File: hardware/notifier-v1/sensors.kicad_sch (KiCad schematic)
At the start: 7 parts, among them U4 BME688, U5 SHT40-AD1B

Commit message: Sensor neck: no plane under island/neck, guarded 0.15 mm bus, wider slot
- In1 GND left out under the sensor island and neck; the neck bus is
  3V3 | GND | SDA | SCL | GND at 0.15 mm, guards joined on B.Cu and
  stitched to In1 below the neck
- Module-side slot widened to 1.8 mm (island side stays 1.2 mm)
- Island hand-routed and locked (deterministic, clear of SHT40 keepout)
- C12 4.7u bulk cap where 3V3 enters the island
- R13 33R in series with LCD_SCLK (new net MCU_LCD_SCLK), GND vias
  beside the SPI layer changes where there is room
- In2 island removal drops slivers between the module thermal vias

Co-Authored-By: Claude Opus 5.5 <noreply@anthropic.com>
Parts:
- added C12: 4.7u, Capacitor_SMD:C_0603_1608Metric, symbol Device:C
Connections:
- net +3V3: now also C12.1
- net GND: now also C12.2
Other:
- note added: "Notes - BME688: gas and pressure only. Its gas heater self-heats, so T/RH come from the SHT40 away from it. - I2C addresses: BME688 0x77 (SDO high), SHT40 0x44. CSB high selects I2C. - 4.7k pull-ups sit at the bus entry; no pours on the sensor island. - C12 4.7u bulk where 3V3 enters the island."
- note removed: "Notes - BME688: gas and pressure only. Its gas heater self-heats, so T/RH come from the SHT40 away from it. - I2C addresses: BME688 0x77 (SDO high), SHT40 0x44. CSB high selects I2C. - 4.7k pull-ups sit at the bus entry; no pours on the sensor island."

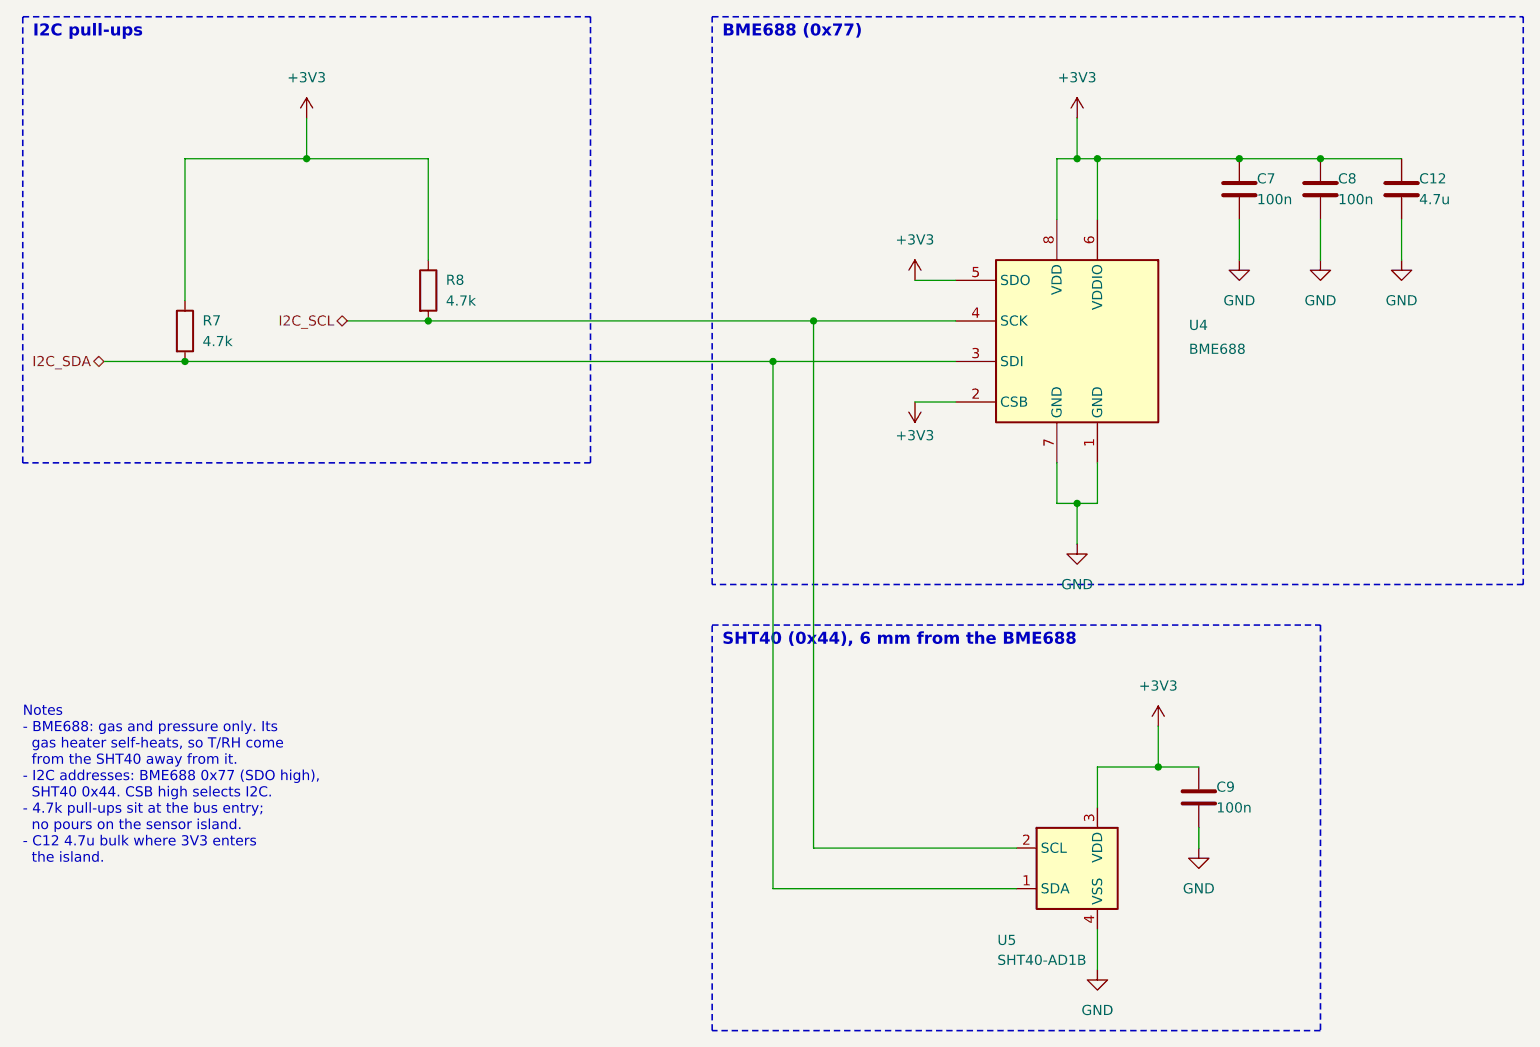
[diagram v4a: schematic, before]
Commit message: Layout A: USB-C on the back edge, corner mounts, no buttons, JLC fab data
- J2 display socket mirrored (1 RST 2 CS 3 DC 4 SDA 5 SCL 6 GND 7 VCC),
  face at the right edge
- USB-C J1 on the left edge (enclosure back), ESD/CC/fuse beside it,
  hand-drawn 0.27/0.15 pair (~91 ohm diff, tools/impedance.py), only
  GND under the shell (DRC rule area)
- SW1-SW3/R6/BTN removed; 1.5 mm debug pads TX RX 3V3 EN GND IO0;
  firmware DESK_BTN = -1 on notifier-v1
- Four M2 corner holes with keepouts; sensor island grown to 14.8 mm
  with H3 in its corner, re-hand-routed (BME688/SHT40 8.9 mm apart)
- I2C >= 1.6 mm from USB on the same layer; vias >= 0.15 mm from
  same-net SMD pads (rule), hand vias >= 0.2 mm
- Silk "v1 ${GIT_SHA}" resolved at fab export; JLC order-number mark
- Fab: Protel gerbers without X2, PTH/NPTH split, JLC BOM/CPL, CPL
  rotation fixes (U4 +90, U5 +270); pipeline --fab-only on a clean
  commit; route retry until the gate passes
- ORDER.md: stackup JLC04161H-7628, rails left/right, preview checklist,
  bring-up without buttons; PLAN.md enclosure notes

Co-Authored-By: Claude Opus 5.5 <noreply@anthropic.com>
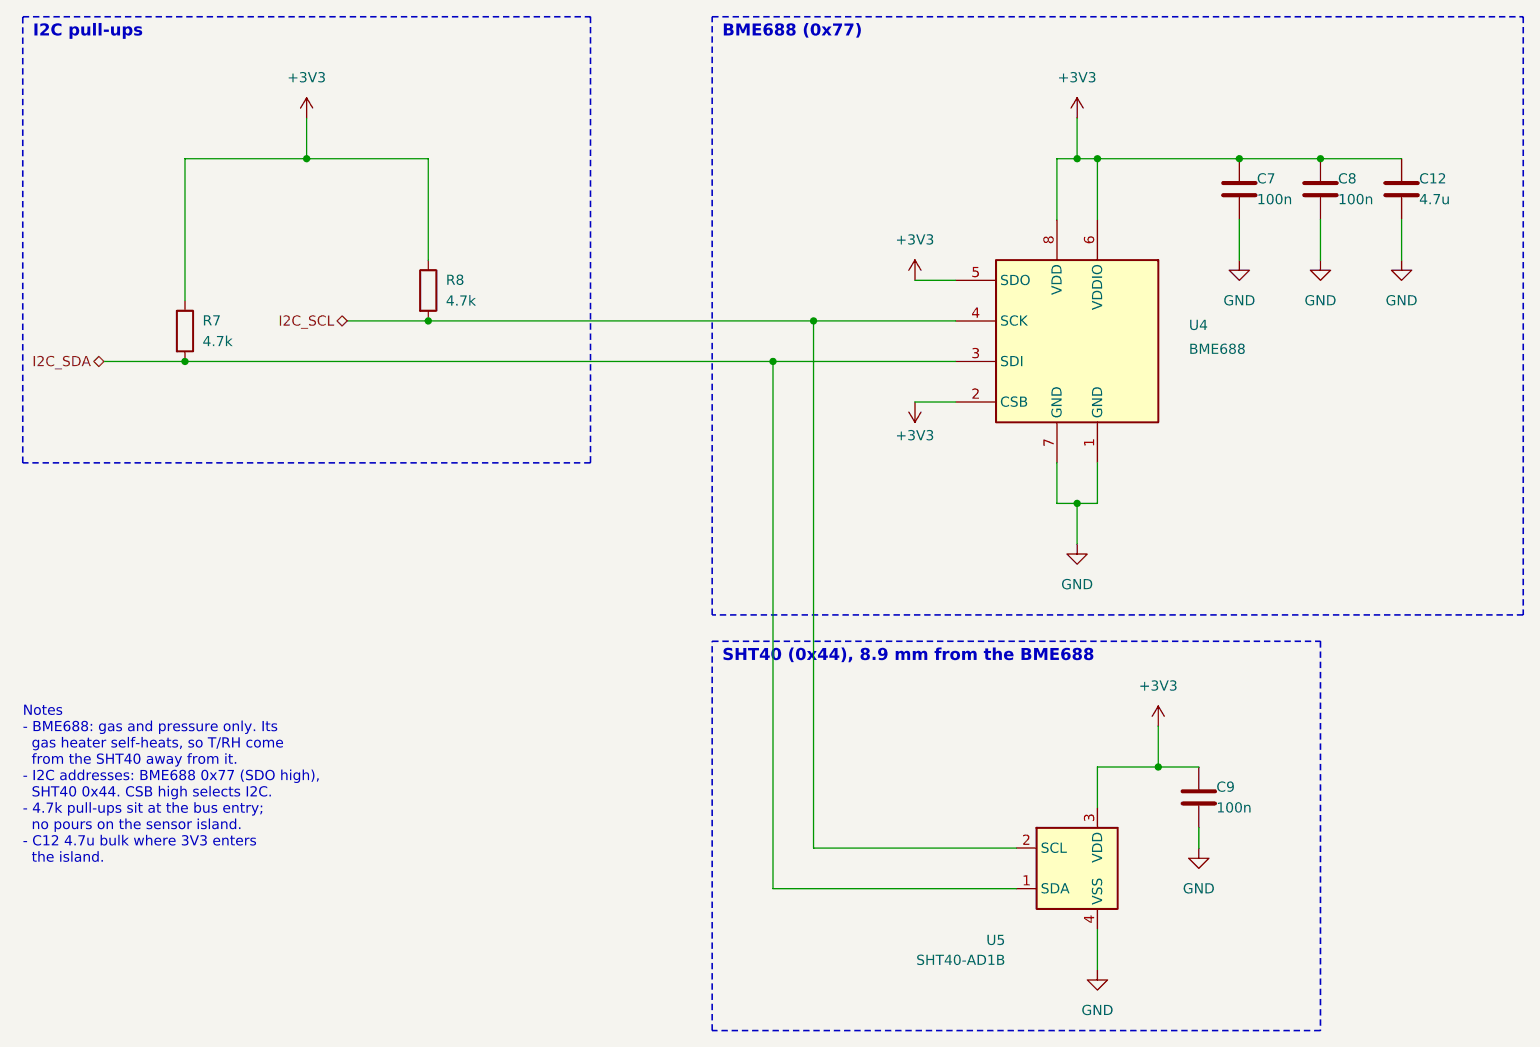
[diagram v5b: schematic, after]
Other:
- note added: "SHT40 (0x44), 8.9 mm from the BME688"
- note removed: "SHT40 (0x44), 6 mm from the BME688"
